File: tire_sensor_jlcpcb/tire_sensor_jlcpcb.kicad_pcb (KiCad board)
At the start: 4 copper layers, 33 x 26 mm, 40 parts, among them J1 Conn_02x05_Odd_Even, U2 DPS368, U3 LIS3DHTR, X1 32MHz, X2 32.768kHz

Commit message: JLCPCB order W2025082300401265
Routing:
- net GND: track 14.5 -> 13.8 mm, vias 115 -> 75

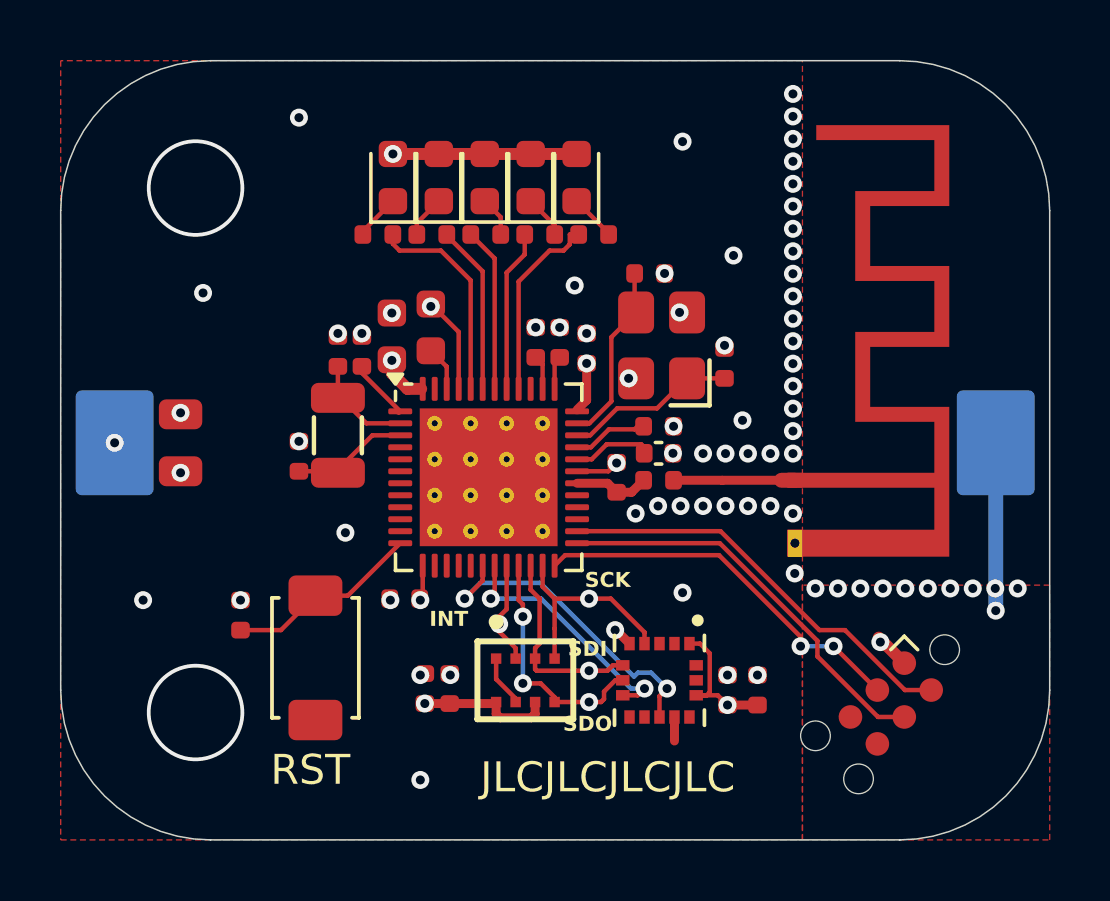
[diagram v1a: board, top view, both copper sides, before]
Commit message: Better routing and decoupling, reomved unused cap
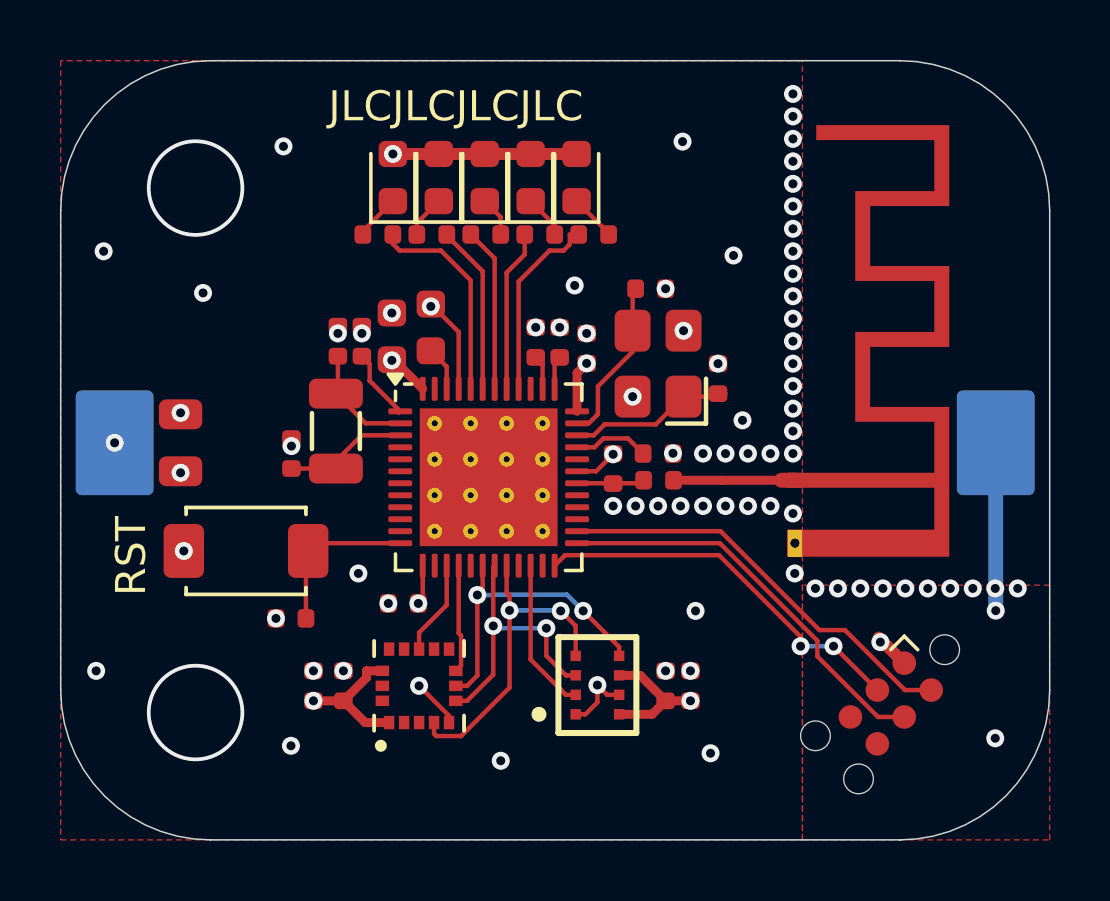
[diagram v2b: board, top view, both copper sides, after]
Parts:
- removed C6: N.C., Capacitor_SMD:C_0402_1005Metric
- moved C16 13.8 mm to (164.2, 112.8)
- moved C17 13.8 mm to (165.2, 112.8)
- moved C18 8.03 mm to (176.8, 112.8)
- moved C19 8.03 mm to (176.0, 112.8)
- moved U3 8.02 mm to (167.8, 112.8), turned to 90 degrees
- moved S1 4.25 mm to (162.0, 108.2), turned to 180 degrees
- moved U2 2.41 mm to (173.7, 112.7), turned to 90 degrees
- moved R6 1.69 mm to (163.5, 110.5), turned to 0 degrees
- moved C7 0.91 mm to (175.8, 105.0)
- moved X1 0.62 mm to (175.8, 102.0)
- moved C1 0.55 mm to (177.8, 102.5)
- moved C2 0.51 mm to (175.5, 99.5)
- moved C11 0.34 mm to (165.1, 101.2)
- moved C4 0.34 mm to (165.9, 101.2)
- moved C3 0.31 mm to (174.2, 105.5)
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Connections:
- U1 pad 15: unconnected-(U1-P0.12-Pad15) -> /INT_LIS3DHTR
- U1 pad 16: unconnected-(U1-P0.13-Pad16) -> /CS_LIS3DHTR
- U1 pad 18: /INT_LIS3DHTR -> /SDO
- U1 pad 19: /CS_LIS3DHTR -> /SDI
- U1 pad 20: /CS_DPS368 -> /SCK
- U1 pad 21: /SDO -> unconnected-(U1-P0.18-Pad21)
- U1 pad 22: /SDI -> /CS_DPS368
- U1 pad 23: /SCK -> unconnected-(U1-P0.20-Pad23)
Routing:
- net /INT_LIS3DHTR: track 10.9 -> 3.17 mm, vias 2 -> 0
- net /CS_LIS3DHTR: track 8.48 -> 3.62 mm, vias 2 -> 0
- net /SCK: track 7.11 -> 11.1 mm, vias 1 -> 2
- net /SDI: track 6.66 -> 9.24 mm, vias 1 -> 2
- net /DEC2: track 2.49 -> 0.00 mm
- net /SDO: track 8.12 -> 10.4 mm, vias 3 -> 2
- net /CS_DPS368: track 3.43 -> 5.12 mm, vias 1 -> 0
- net /BTN: track 6.53 -> 5.46 mm
- net /DEC1: track 2.20 -> 2.76 mm
- net /XC2: track 6.08 -> 5.53 mm
- net GND: track 13.8 -> 14.2 mm, vias 75 -> 81
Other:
- board text removed: "INT"
- board text removed: "SCK"
- board text removed: "SDI"
- board text removed: "SDO"

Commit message: Added extra GND trace
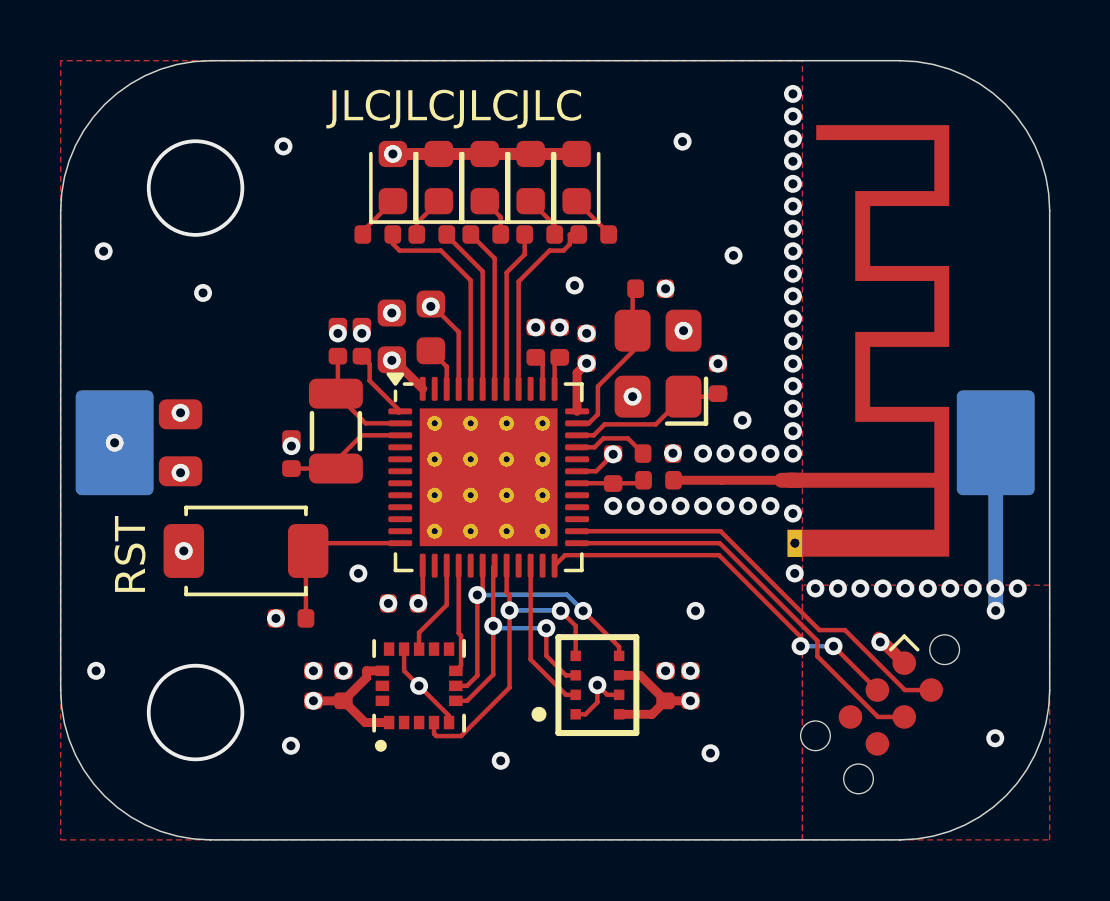
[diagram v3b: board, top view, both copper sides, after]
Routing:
- net GND: track 14.2 -> 15.7 mm
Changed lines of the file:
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@@
+	)
+	(segment
+		(start 167.275 111.525)
+		(end 167.275 112.25)
+		(width 0.15)
+		(layer "F.Cu")
+		(net 3)
+	)
+	(segment
+		(start 167.275 112.25)
+		(end 167.775 112.75)
+		(width 0.15)
+		(layer "F.Cu")
+		(net 3)
 	)
 	(segment

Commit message: Add gyro, reroute sensors
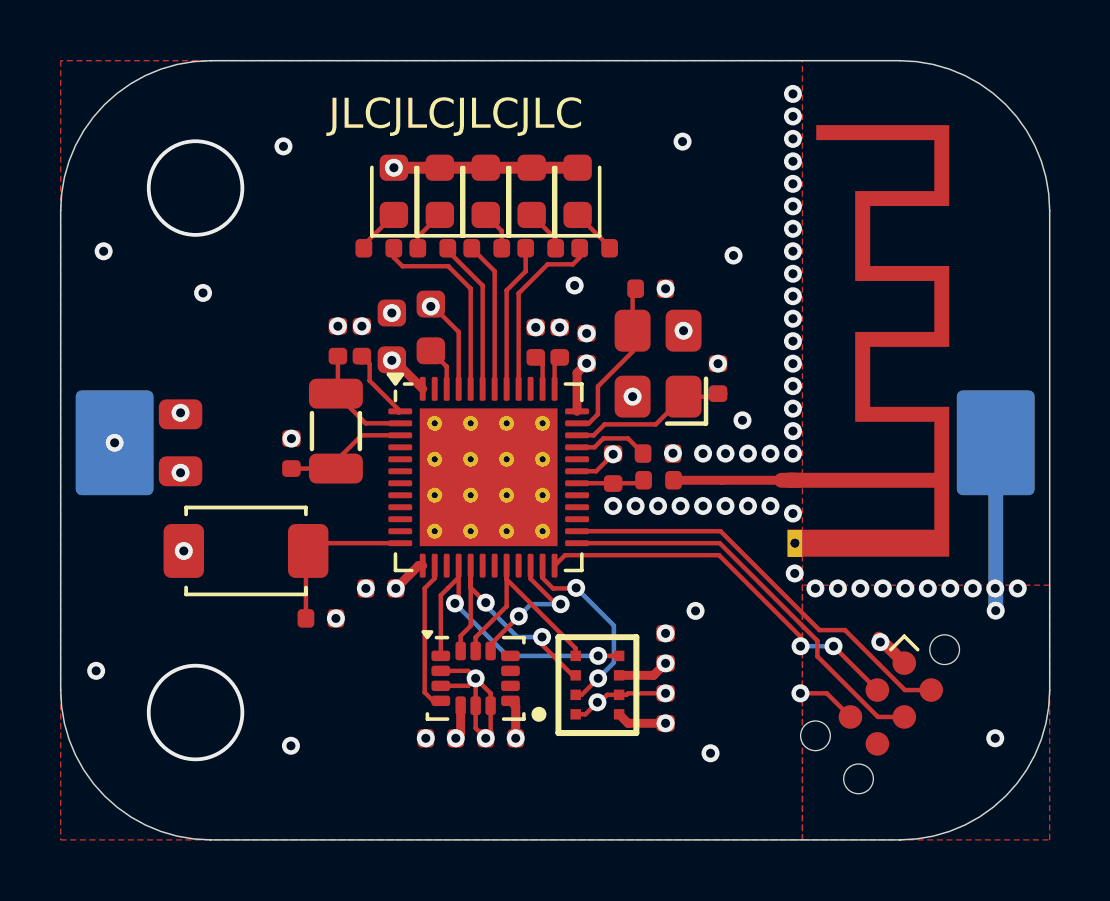
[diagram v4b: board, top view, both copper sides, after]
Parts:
- C19: value 10uF -> 100nF
- U3: value LIS3DHTR -> LSM6DS3; footprint footprints:XDCR_LIS3DHTR -> Package_LGA:LGA-14_3x2.5mm_P0.5mm_LayoutBorder3x4y
- moved C16 6.49 mm to (170.5, 114.5), turned to 180 degrees
- moved C17 3.69 mm to (168.5, 114.5), turned to 180 degrees
- moved U3 1.90 mm to (169.7, 112.5), turned to 0 degrees
- moved C19 1.25 mm to (176.0, 111.5)
- moved C18 1.12 mm to (176.0, 113.5)
- moved R6 1.00 mm to (164.5, 110.5), turned to 180 degrees
- moved C5 0.90 mm to (166.5, 109.5)
- moved D2 0.46 mm to (171.5, 96.2)
- moved D3 0.46 mm to (170.0, 96.2)
- moved D4 0.46 mm to (168.5, 96.2)
- moved D5 0.46 mm to (166.9, 96.2)
- moved R2 0.46 mm to (171.8, 98.2)
- moved R3 0.46 mm to (170.0, 98.2)
- moved R5 0.46 mm to (166.4, 98.2)
- moved D1 0.46 mm to (173.1, 96.2)
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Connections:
- U1 pad 14: unconnected-(U1-P0.11-Pad14) -> /INT_LSM6DS3
- U1 pad 15: /INT_LIS3DHTR -> unconnected-(U1-P0.12-Pad15)
- U1 pad 16: /CS_LIS3DHTR -> /SDO
- U1 pad 17: unconnected-(U1-P0.14-Pad17) -> /SDI
- U1 pad 18: /SDO -> unconnected-(U1-P0.15-Pad18)
- U1 pad 19: /SDI -> unconnected-(U1-P0.16-Pad19)
- U1 pad 22: /CS_DPS368 -> /CS_LSM6DS3
- U1 pad 23: unconnected-(U1-P0.20-Pad23) -> /CS_DPS368
- U3 pad 1: VDD_NRF -> /SDO
- U3 pad 11: /INT_LIS3DHTR -> unconnected-(U3-NC-Pad11)
- U3 pad 12: GND -> /CS_LSM6DS3
- U3 pad 13: unconnected-(U3-ADC3-Pad13) -> /SCK
- U3 pad 14: VDD_NRF -> /SDI
- U3 pad 2: (no net) -> GND
- U3 pad 3: (no net) -> GND
- U3 pad 4: /SCK -> /INT_LSM6DS3
- U3 pad 5: GND -> VDD_NRF
- U3 pad 6: /SDI -> GND
- U3 pad 7: /SDO -> GND
- U3 pad 8: /CS_LIS3DHTR -> VDD_NRF
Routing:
- net GND: track 15.7 -> 22.5 mm, vias 81 -> 80
- net /INT_LSM6DS3: track 0.00 -> 5.02 mm
- net /CS_LSM6DS3: track 0.00 -> 4.90 mm, vias 0 -> 2
- net /SCK: track 11.1 -> 7.24 mm, vias 2 -> 0
- net /CS_LIS3DHTR: track 3.62 -> 0.00 mm
- net VDD_NRF: track 22.5 -> 19.2 mm, vias 10 -> 12
- net /INT_LIS3DHTR: track 3.17 -> 0.00 mm
- net /CS_DPS368: track 5.12 -> 6.42 mm, vias 0 -> 2
- net /SDI: track 9.24 -> 8.64 mm
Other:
- board text removed: "RST"

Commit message: JLCPCB order W2025111310437228
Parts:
- removed D5: LED, LED_SMD:LED_0603_1608Metric
- removed R5: 1kΩ, PCM_JLCPCB:R_0402
- X1: value 32MHz -> NX2016SA-32MHZ-EXS00A-CS06654; footprint PCM_JLCPCB:OSC-SMD_4P-L3.2-W2.5-BL_SIT8008BI -> footprints:NX2016SA_NDK
- moved J1 23.1 mm to (160.4, 113.4), turned to 135 degrees
- moved C15 7.16 mm to (162.8, 98.1), turned to 55 degrees
- moved R6 5.35 mm to (161.1, 106.4), turned to -90 degrees
- moved S1 4.63 mm to (158.8, 104.9), turned to 90 degrees
- moved AE1 1.63 mm to (181.9, 105.9)
- moved C2 1.22 mm to (175.1, 100.6)
- moved C1 0.94 mm to (176.8, 102.6)
- moved X1 0.85 mm to (175.1, 102.5), turned to 180 degrees
- moved BT1 0.46 mm to (171.9, 104.6), turned to -35 degrees
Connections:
- U1 pad 44: /LED4 -> unconnected-(U1-N.C.-Pad44)
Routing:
- net /SWDIO: track 14.0 -> 20.8 mm, vias 0 -> 2
- net /LED4: track 6.65 -> 0.00 mm
- net /SWCLK: track 13.6 -> 18.3 mm, vias 0 -> 2
- net /nRESET: track 13.0 -> 17.5 mm
- net GND: track 22.5 -> 19.1 mm, vias 80 -> 73
- net /BTN: track 5.46 -> 8.82 mm
- net VDD_NRF: track 19.2 -> 16.8 mm
- net /RF: track 4.12 -> 5.75 mm
- net Net-(D5-K): track 1.53 -> 0.00 mm
- net /XC2: track 5.53 -> 4.21 mm
- net /XC1: track 5.53 -> 4.41 mm
- added copper zone on B.Cu, net GND
- removed copper zone on In1.Cu, net GND
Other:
- outline, holes or cut-outs redrawn
- board text added: "rev b @wadetb"

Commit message: RF trace fixes from DevZone
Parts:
- moved C7 0.42 mm to (175.7, 104.6)
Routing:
- net GND: track 19.1 -> 22.0 mm, vias 73 -> 69
- added copper zone on In1.Cu, net GND
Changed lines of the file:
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@@
 	(footprint "PCM_JLCPCB:C_0402"
 		(layer "F.Cu")
-		(at 175.75 105)
+		(at 175.66656 104.590685)
 		(descr "Capacitor SMD 0402 (1005 Metric), square (rectangular) end terminal, IPC_7351 nominal, (Body size source: IPC-SM-782 page 76, https://www.pcb-3d.com/wordpress/wp-content/uploads/ipc-sm-782a_amendment_1_and_2.pdf), generated with kicad-footprint-generator")
 		(tags "capacitor")
@@
 	)
 	(segment
+		(start 170.29656 105.590685)
+		(end 170.09656 105.790685)
+		(width 0.15)
+		(layer "F.Cu")
+		(net 3)
+	)
+	(segment
 		(start 170.1625 113.4125)
 		(end 170.1625 113)
@@
 	(segment
 		(start 173.04656 105.590685)
+		(end 170.29656 105.590685)
+		(width 0.15)
+		(layer "F.Cu")
+		(net 3)
+	)
+	(segment
+		(start 173.04656 105.590685)
 		(end 173.684315 105.590685)
 		(width 0.15)
@@
 	)
 	(via
-		(at 176.5 106.75)
+		(at 177.06656 106.990685)
 		(size 0.6)
 		(drill 0.3)
@@
 	)
 	(via
-		(at 178.75 106.75)
+		(at 179.31656 106.990685)
 		(size 0.6)
 		(drill 0.3)
@@
 	)
 	(via
-		(at 175 106.75)
+		(at 175.56656 106.990685)
 		(size 0.6)
 		(drill 0.3)
@@
 	)
 	(via
-		(at 180.25 105)
-		(size 0.6)
-		(drill 0.3)
-		(layers "F.Cu" "B.Cu")
-		(free yes)
-		(net 3)
-	)
-	(via
 		(at 180.25 104.25)
 		(size 0.6)
@@
 	)
 	(via
-		(at 178 106.75)
+		(at 178.56656 106.990685)
 		(size 0.6)
 		(drill 0.3)
@@
 	)
 	(via
-		(at 179.5 105)
+		(at 179.5 104.790685)
 		(size 0.6)
 		(drill 0.3)
@@
 	)
 	(via
-		(at 177.25 106.75)
+		(at 177.81656 106.990685)
 		(size 0.6)
 		(drill 0.3)
@@
 	)
 	(via
-		(at 178 105)
-		(size 0.6)
-		(drill 0.3)
-		(layers "F.Cu" "B.Cu")
-		(free yes)
-		(net 3)
-	)
-	(via
-		(at 180.25 107)
+		(at 178 104.790685)
 		(size 0.6)
 		(drill 0.3)
@@
 	)
 	(via
-		(at 174.25 105.025)
-		(size 0.6)
-		(drill 0.3)
-		(layers "F.Cu" "B.Cu")
-		(free yes)
-		(net 3)
-	)
-	(via
 		(at 160.81656 110.140685)
 		(size 0.6)
@@
 	)
 	(via
-		(at 179.5 106.75)
+		(at 180.06656 106.990685)
 		(size 0.6)
 		(drill 0.3)
@@
 	)
 	(via
-		(at 177.25 105)
+		(at 177.25 104.790685)
 		(size 0.6)
 		(drill 0.3)
@@
 	)
 	(via
-		(at 180.06656 107.890685)
+		(at 180.175875 108)
 		(size 0.6)
 		(drill 0.3)
@@
 	)
 	(via
-		(at 178.75 105)
+		(at 178.75 104.790685)
 		(size 0.6)
 		(drill 0.3)
@@
 	)
 	(via
-		(at 175.75 106.75)
+		(at 176.31656 106.990685)
 		(size 0.6)
 		(drill 0.3)
@@
 	)
 	(via
-		(at 174.25 106.75)
-		(size 0.6)
-		(drill 0.3)
-		(layers "F.Cu" "B.Cu")
-		(free yes)
-		(net 3)
-	)
-	(via
-		(at 176.24656 104.990685)
+		(at 176.16656 104.590685)
 		(size 0.6)
 		(drill 0.3)
@@
 	)
 	(segment
-		(start 180.175875 108)
-		(end 180.06656 107.890685)
-		(width 0.15)
-		(layer "B.Cu")
-		(net 3)
-	)
-	(segment
 		(start 181.94156 108)
 		(end 180.175875 108)
@@
 	)
 	(segment
-		(start 173.627833 104.790685)
-		(end 173.924518 104.494)
+		(start 173.924518 104.494)
+		(end 175.069875 104.494)
 		(width 0.15)
 		(layer "F.Cu")
@@
 	)
 	(segment
-		(start 174.744 104.494)
-		(end 175.25 105)
+		(start 173.04656 104.790685)
+		(end 173.627833 104.790685)
 		(width 0.15)
 		(layer "F.Cu")
@@
 	)
 	(segment
-		(start 173.924518 104.494)
-		(end 174.744 104.494)
+		(start 175.069875 104.494)
+		(end 175.16656 104.590685)
 		(width 0.15)
 		(layer "F.Cu")
@@
 	)
 	(segment
-		(start 173.04656 104.790685)
-		(end 173.627833 104.790685)
+		(start 173.627833 104.790685)
+		(end 173.924518 104.494)
 		(width 0.15)
 		(layer "F.Cu")
@@
 	)
 	(segment
-		(start 179.86656 105.890685)
-		(end 179.875875 105.9)
-		(width 0.3)
-		(layer "F.Cu")
-		(net 17)
-	)
-	(segment
-		(start 179.875875 105.9)
+		(start 181.932245 105.890685)
 		(end 181.94156 105.9)
 		(width 0.3)
@@
 	)
 	(segment
-		(start 176.19656 105.890685)
-		(end 179.86656 105.890685)
-		(width 0.3)
+		(start 176.26656 105.890685)
+		(end 181.932245 105.890685)
+		(width 1)
 		(layer "F.Cu")
 		(net 17)
@@
 		(net 3)
 		(net_name "GND")
-		(locked yes)
-		(layers "F.Cu" "B.Cu")
+		(layers "F.Cu" "B.Cu" "In1.Cu")
 		(hatch edge 0.5)
 		(priority 1)
@@
 		(net 3)
 		(net_name "GND")
-		(locked yes)
-		(layers "F.Cu" "B.Cu")
+		(layers "F.Cu" "B.Cu" "In1.Cu")
 		(hatch edge 0.5)
 		(priority 1002)
 		(connect_pads
-			(clearance 0.5)
+			(clearance 0.15)
 		)
 		(min_thickness 0.25)
@@
 			)
 		)
+	)
+	(zone
+		(net 0)
+		(net_name "")
+		(layers "In1.Cu" "In2.Cu")
+		(hatch edge 0.5)
+		(connect_pads
+			(clearance 0)
+		)
+		(min_thickness 0.25)
+		(filled_areas_thickness no)
+		(keepout
+			(tracks allowed)
+			(vias allowed)
+			(pads allowed)
+			(copperpour not_allowed)
+			(footprints allowed)
+		)
+		(placement
+			(enabled no)
+			(sheetname "/")
+		)
+		(fill
+			(thermal_gap 0.5)
+			(thermal_bridge_width 0.5)
+		)
+		(polygon
+			(pts
+				(xy 180.76656 106.590685) (xy 173.76656 106.590685) (xy 173.76656 105.190685) (xy 180.76656 105.190685)
+			)
+		)
